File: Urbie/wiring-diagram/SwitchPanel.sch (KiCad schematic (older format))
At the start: 12 parts

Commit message: Organizing relay box sheet
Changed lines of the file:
@@
 	8000 3650 5900 3650
-Wire Wire Line
-	6300 3350 7400 3350
-Wire Wire Line
-	7400 3350 7400 3300
-Wire Wire Line
-	7400 3300 7350 3300
-Wire Wire Line
-	7350 3300 7350 3350
-Connection ~ 7350 3350
 Wire Wire Line
 	5800 3000 5800 3750
@@
 Wire Wire Line
 	6300 1850 6300 3350
-Wire Wire Line
-	8500 2250 8500 2250
 Wire Wire Line
 	7200 1300 7200 2250
@@
 Text Label 8650 2850 2    60   ~ 0
 EFI
+Wire Wire Line
+	6300 3350 7350 3350
 $EndSCHEMATC

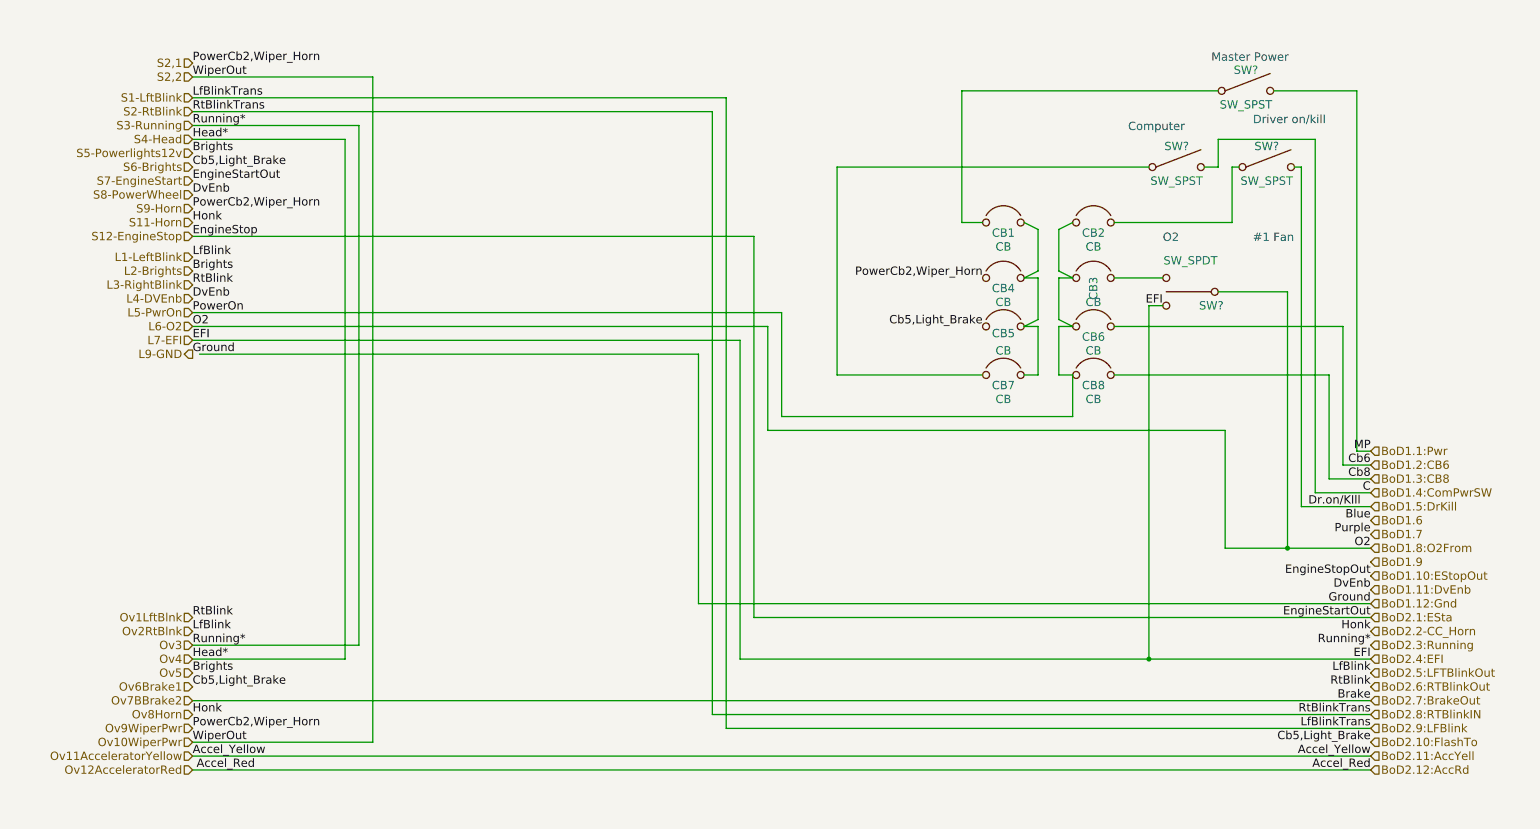
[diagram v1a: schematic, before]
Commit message: cleaning up schematics
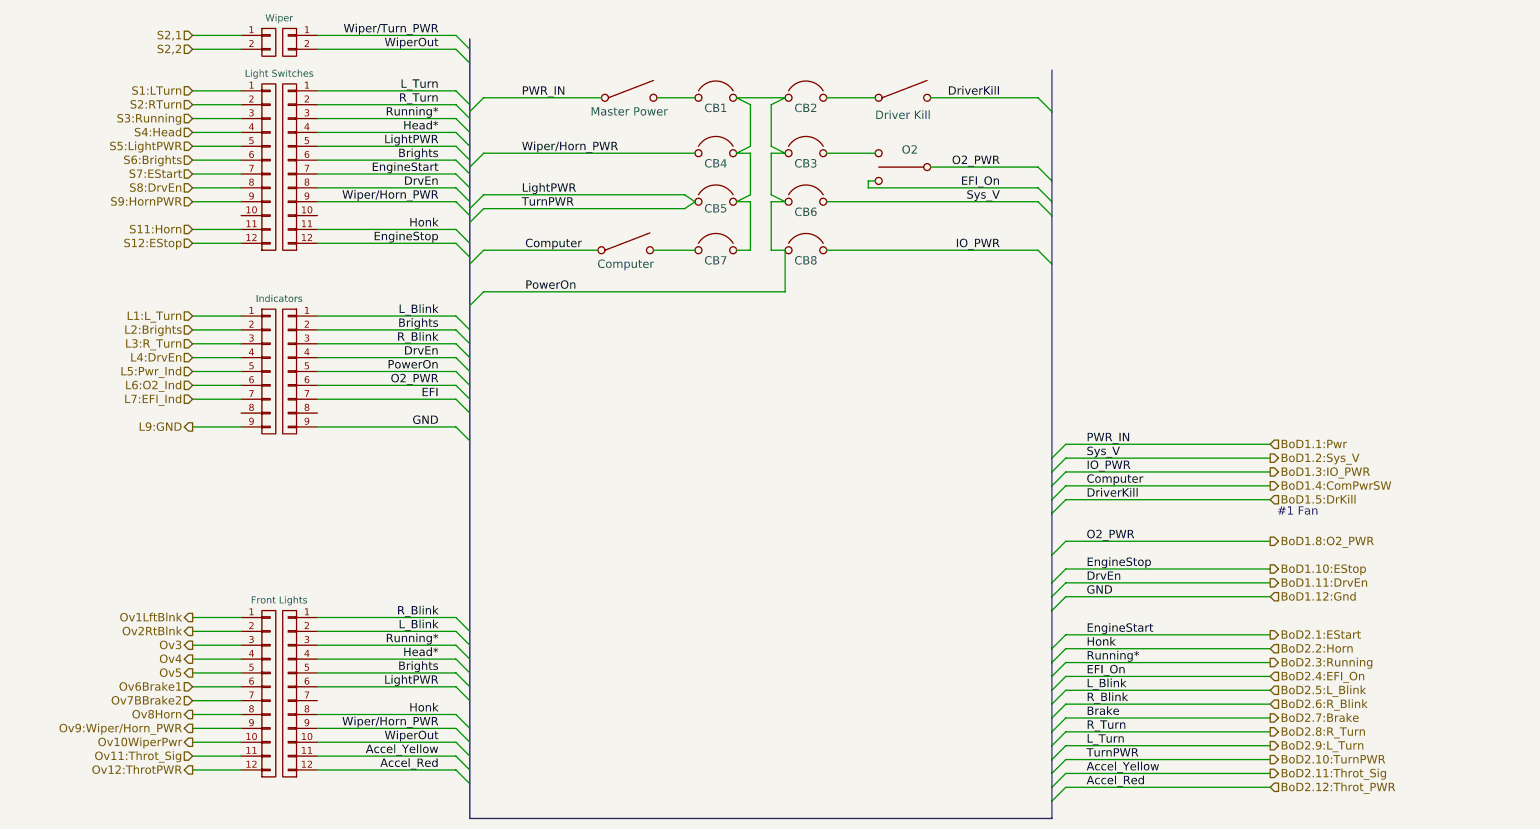
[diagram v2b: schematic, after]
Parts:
- added P?: CONN_01X09, symbol CONN_01X09
- added P?: Indicators, symbol CONN_01X09
- added P? (x2): CONN_01X12, symbol CONN_01X12
- added P?: Light Switches, symbol CONN_01X12
- added P?: CONN_01X02, symbol CONN_01X02
- added P?: Wiper, symbol CONN_01X02
- added P?: Front Lights, symbol CONN_01X12
- SW?: value SW_SPST -> Master Power
- SW?: value SW_SPST -> Computer
- SW?: value SW_SPST -> Driver Kill
- SW?: value SW_SPDT -> O2
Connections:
- net L5-PwrOn is gone; now on net PowerOn: CB2.1 (Line), CB3.1 (Line), CB6.1 (Line), CB8.1 (Line)
- net BoD1.12:Gnd: now also P?.9 (P9)
- net BoD1.1:Pwr: now also SW?.1; no longer SW?.2
- net BoD1.4:ComPwrSW: now also SW?.1; no longer SW?.2
- net BoD2.3:Running: now also P?.3 (P3), P?.3 (P3)
- net Ov10WiperPwr: now also P?.10 (P10)
- net Ov4: now also P?.4 (P4)
- net at CB1.1 (Line): now also SW?.2; no longer SW?.1
- net PowerOn: now reaches CB1.2 (Load), CB4.2 (Load), CB5.2 (Load), CB7.2 (Load)
- net PowerOn: now also P?.5 (P5)
- net at CB7.1 (Line): now also SW?.2; no longer SW?.1
- net BoD1.2:CB6 renamed BoD1.2:Sys_V
- net BoD1.3:CB8 renamed BoD1.3:IO_PWR
- net BoD1.8:O2From renamed BoD1.8:O2_PWR
- net BoD1.8:O2_PWR: now also P?.6 (P6)
- net BoD2.10:FlashTo renamed BoD2.10:TurnPWR
- net BoD2.10:TurnPWR: now also P?.5 (P5), P?.6 (P6)
- net BoD2.4:EFI renamed BoD2.4:EFI_On
- net Ov9WiperPwr renamed Wiper/Horn_PWR
- net Wiper/Horn_PWR: now also P?.9 (P9), P?.9 (P9)
- new net BoD1.10:EStop: P?.12 (P12)
- new net BoD1.11:DrvEn: P?.4 (P4), P?.8 (P8)
- new net BoD2.11:Throt_Sig: P?.11 (P11)
- new net BoD2.12:Throt_PWR: P?.12 (P12)
- new net BoD2.1:EStart: P?.7 (P7)
- new net BoD2.2:Horn: P?.11 (P11), P?.8 (P8)
- new net BoD2.5:L_Blink: P?.1 (P1), P?.2 (P2)
- new net BoD2.6:R_Blink: P?.1 (P1), P?.3 (P3)
- new net BoD2.8:R_Turn: P?.2 (P2)
- new net BoD2.9:L_Turn: P?.1 (P1)
- new net Brights: P?.2 (P2), P?.5 (P5), P?.6 (P6)
- new net EFI: P?.7 (P7)
- new net Head*: P?.4 (P4), P?.4 (P4)
- new net L1:L_Turn: P?.1 (P1)
- new net L2:Brights: P?.2 (P2)
- new net L3:R_Turn: P?.3 (P3)
- new net L4:DrvEn: P?.4 (P4)
- new net L5:Pwr_Ind: P?.5 (P5)
- new net L6:O2_Ind: P?.6 (P6)
- new net L7:EFI_Ind: P?.7 (P7)
- new net L9:GND: P?.9 (P9)
- new net Ov11:Throt_Sig: P?.11 (P11)
- new net Ov12:ThrotPWR: P?.12 (P12)
- new net Ov1LftBlnk: P?.1 (P1)
- new net Ov2RtBlnk: P?.2 (P2)
- new net Ov3: P?.3 (P3)
- new net Ov5: P?.5 (P5)
- new net Ov6Brake1: P?.6 (P6)
- new net Ov7BBrake2: P?.7 (P7)
- new net Ov8Horn: P?.8 (P8)
- new net Ov9:Wiper/Horn_PWR: P?.9 (P9)
- new net S11:Horn: P?.11 (P11)
- new net S12:EStop: P?.12 (P12)
- new net S1:LTurn: P?.1 (P1)
- new net S2,1: P?.1 (P1)
- new net S2,2: P?.2 (P2)
- new net S2:RTurn: P?.2 (P2)
- new net S3:Running: P?.3 (P3)
- new net S4:Head: P?.4 (P4)
- new net S5:LightPWR: P?.5 (P5)
- new net S6:Brights: P?.6 (P6)
- new net S7:EStart: P?.7 (P7)
- new net S8:DrvEn: P?.8 (P8)
- new net S9:HornPWR: P?.9 (P9)
- new net Wiper/Turn_PWR: P?.1 (P1)
- new net WiperOut: P?.10 (P10), P?.2 (P2)
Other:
- note removed: "Computer"
- note removed: "Driver on/kill"
- note removed: "Master Power"
- note removed: "O2"
- moved on the sheet: CB1, CB2, CB3, CB4, CB5, CB6, CB7, CB8

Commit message: fixed some stuff
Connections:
- net BoD2.7:Brake: now also P?.7 (P7)
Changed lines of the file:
@@
 $Descr USLetter 11000 8500
 encoding utf-8
-Sheet 9 9
+Sheet 9 13
 Title "Urbie - Switch Panel"
 Date "2017-01-07"
@@
 Wire Wire Line
 	2550 6000 3550 6000
+Text Label 3425 5700 2    60   ~ 0
+Brake
+Wire Wire Line
+	2550 5700 3550 5700
+Entry Wire Line
+	3550 5700 3650 5800
 $EndSCHEMATC

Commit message: updated 1593BB-box footprint
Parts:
- removed P?: CONN_01X12, symbol CONN_01X12
- removed P?: Front Lights, symbol CONN_01X12
- added P? (x2): CONN_01X15, symbol CONN_01X15
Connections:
- net BoD1.12:Gnd: now also P?.13 (P13), P?.14 (P14), P?.15 (P15)
- net BoD2.10:TurnPWR: now also P?.6 (P6)
- net BoD2.11:Throt_Sig: now also P?.11 (P11)
- net BoD2.12:Throt_PWR: now also P?.12 (P12)
- net BoD2.2:Horn: now also P?.8 (P8)
- net BoD2.3:Running: now also P?.3 (P3)
- net BoD2.5:L_Blink: now also P?.2 (P2)
- net BoD2.6:R_Blink: now also P?.1 (P1)
- net BoD2.7:Brake: now also P?.7 (P7)
- net Brights: now also P?.5 (P5)
- net Head*: now also P?.4 (P4)
- net Ov10WiperPwr: now also P?.10 (P10)
- net Ov11:Throt_Sig: now also P?.11 (P11)
- net Ov12:ThrotPWR: now also P?.12 (P12)
- net Ov1LftBlnk: now also P?.1 (P1)
- net Ov2RtBlnk: now also P?.2 (P2)
- net Ov3: now also P?.3 (P3)
- net Ov4: now also P?.4 (P4)
- net Ov5: now also P?.5 (P5)
- net Ov6Brake1: now also P?.6 (P6)
- net Ov7BBrake2: now also P?.7 (P7)
- net Ov8Horn: now also P?.8 (P8)
- net Ov9:Wiper/Horn_PWR: now also P?.9 (P9)
- net Wiper/Horn_PWR: now also P?.9 (P9)
- net WiperOut: now also P?.10 (P10)
- new net Ov13:GND: P?.13 (P13)
- new net Ov14:GND: P?.14 (P14)
- new net Ov15:GND: P?.15 (P15)
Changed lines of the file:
@@
 $Descr USLetter 11000 8500
 encoding utf-8
-Sheet 9 13
+Sheet 13 13
 Title "Urbie - Switch Panel"
 Date "2017-01-07"
@@
 Comment4 ""
 $EndDescr
+Text HLabel 1650 4900 0    60   Output ~ 0
+Ov1LftBlnk
+Text HLabel 1650 5000 0    60   Output ~ 0
+Ov2RtBlnk
 Text HLabel 1650 5100 0    60   Output ~ 0
-Ov1LftBlnk
+Ov3
 Text HLabel 1650 5200 0    60   Output ~ 0
-Ov2RtBlnk
+Ov4
 Text HLabel 1650 5300 0    60   Output ~ 0
-Ov3
-Text HLabel 1650 5400 0    60   Output ~ 0
-Ov4
-Text HLabel 1650 5500 0    60   Output ~ 0
 Ov5
-Text HLabel 1650 5600 0    60   Input ~ 0
+Text HLabel 1650 5400 0    60   Input ~ 0
 Ov6Brake1
-Text HLabel 1650 5700 0    60   Input ~ 0
+Text HLabel 1650 5500 0    60   Input ~ 0
 Ov7BBrake2
+Text HLabel 1650 5600 0    60   Output ~ 0
+Ov8Horn
+Text HLabel 1650 5700 0    60   Output ~ 0
+Ov9:Wiper/Horn_PWR
 Text HLabel 1650 5800 0    60   Output ~ 0
-Ov8Horn
-Text HLabel 1650 5900 0    60   Output ~ 0
-Ov9:Wiper/Horn_PWR
+Ov10WiperPwr
+Text HLabel 1650 5900 0    60   Input ~ 0
+Ov11:Throt_Sig
 Text HLabel 1650 6000 0    60   Output ~ 0
-Ov10WiperPwr
-Text HLabel 1650 6100 0    60   Input ~ 0
-Ov11:Throt_Sig
-Text HLabel 1650 6200 0    60   Output ~ 0
 Ov12:ThrotPWR
 Text HLabel 1650 2925 0    60   Input ~ 0
@@
 Text Label 3425 1700 2    60   ~ 0
 LightPWR
-Text Label 3425 5600 2    60   ~ 0
+Text Label 3425 5400 2    60   ~ 0
 LightPWR
 Text Label 8100 6125 0    60   ~ 0
@@
 Text Label 3425 2300 2    60   ~ 0
 Honk
-Text Label 3425 5800 2    60   ~ 0
+Text Label 3425 5600 2    60   ~ 0
 Honk
 Text Label 8100 5325 0    60   ~ 0
@@
 Text Label 3425 2925 2    60   ~ 0
 L_Blink
-Text Label 3425 5200 2    60   ~ 0
+Text Label 3425 5000 2    60   ~ 0
 L_Blink
 Text Label 8100 5625 0    60   ~ 0
@@
 Text Label 3425 3025 2    60   ~ 0
 Brights
-Text Label 3425 5500 2    60   ~ 0
+Text Label 3425 5300 2    60   ~ 0
 Brights
-Text Label 3425 5100 2    60   ~ 0
+Text Label 3425 4900 2    60   ~ 0
 R_Blink
 Text Label 3425 3125 2    60   ~ 0
@@
 Text Label 3425 1500 2    60   ~ 0
 Running*
-Text Label 3425 5300 2    60   ~ 0
+Text Label 3425 5100 2    60   ~ 0
 Running*
 Text Label 8100 5425 0    60   ~ 0
@@
 Text Label 3425 1600 2    60   ~ 0
 Head*
-Text Label 3425 5400 2    60   ~ 0
+Text Label 3425 5200 2    60   ~ 0
 Head*
-Text Label 3425 5900 2    60   ~ 0
+Text Label 3425 5700 2    60   ~ 0
 Wiper/Horn_PWR
 Text Label 3425 1000 2    60   ~ 0
 WiperOut
-Text Label 3425 6000 2    60   ~ 0
+Text Label 3425 5800 2    60   ~ 0
 WiperOut
 Text Label 8100 4750 0    60   ~ 0
@@
 Text Label 8100 6325 0    60   ~ 0
 Accel_Red
-Text Label 3425 6200 2    60   ~ 0
+Text Label 3425 6000 2    60   ~ 0
 Accel_Red
-Text Label 3425 6100 2    60   ~ 0
+Text Label 3425 5900 2    60   ~ 0
 Accel_Yellow
 Text Label 3425 2400 2    60   ~ 0
@@
 	3550 3725 3650 3825
 Entry Wire Line
+	3550 4900 3650 5000
+Entry Wire Line
+	3550 5000 3650 5100
+Entry Wire Line
 	3550 5100 3650 5200
 Entry Wire Line
@@
 	3550 5400 3650 5500
 Entry Wire Line
-	3550 5500 3650 5600
-Entry Wire Line
 	3550 5600 3650 5700
 Entry Wire Line
+	3550 5700 3650 5800
+Entry Wire Line
 	3550 5800 3650 5900
 Entry Wire Line
@@
 Entry Wire Line
 	3550 6000 3650 6100
-Entry Wire Line
-	3550 6100 3650 6200
-Entry Wire Line
-	3550 6200 3650 6300
 $Comp
 L CONN_01X09 P?
@@
 Wire Wire Line
 	2000 1000 1650 1000
-$Comp
-L CONN_01X12 P?
-U 1 1 58784560
-P 2350 5650
-F 0 "P?" H 2350 6300 50  0001 C CNN
-F 1 "CONN_01X12" V 2450 5650 50  0001 C CNN
-F 2 "" H 2350 5650 50  0000 C CNN
-F 3 "" H 2350 5650 50  0000 C CNN
-	1    2350 5650
+Wire Wire Line
+	2550 4900 3550 4900
+Wire Wire Line
+	2550 5000 3550 5000
+Wire Wire Line
+	2550 5100 3550 5100
+Wire Wire Line
+	2550 5200 3550 5200
+Wire Wire Line
+	2550 5300 3550 5300
+Wire Wire Line
+	2550 5400 3550 5400
+Wire Wire Line
+	2550 5600 3550 5600
+Wire Wire Line
+	2550 5700 3550 5700
+Wire Wire Line
+	2550 5900 3550 5900
+Wire Wire Line
+	2550 6000 3550 6000
+Wire Wire Line
+	2000 6000 1650 6000
+Wire Wire Line
+	1650 5900 2000 5900
+Wire Wire Line
+	1650 5700 2000 5700
+Wire Wire Line
+	1650 5600 2000 5600
+Wire Wire Line
+	1650 5500 2000 5500
+Wire Wire Line
+	1650 5400 2000 5400
+Wire Wire Line
+	1650 5300 2000 5300
+Wire Wire Line
+	1650 5200 2000 5200
+Wire Wire Line
+	1650 5100 2000 5100
+Wire Wire Line
+	1650 5000 2000 5000
+Wire Wire Line
+	1650 4900 2000 4900
+Wire Wire Line
+	2000 5800 1650 5800
+Wire Wire Line
+	2550 5800 3550 5800
+Text Label 3425 5500 2    60   ~ 0
+Brake
+Wire Wire Line
+	2550 5500 3550 5500
+Entry Wire Line
+	3550 5500 3650 5600
+$Comp
+L CONN_01X15 P?
+U 1 1 5891B89E
+P 2200 5600
+F 0 "P?" H 2200 6400 50  0000 C CNN
+F 1 "CONN_01X15" V 2300 5600 50  0001 C CNN
+F 2 "" H 2200 5600 50  0000 C CNN
+F 3 "" H 2200 5600 50  0000 C CNN
+	1    2200 5600
+	1    0    0    -1
+$EndComp
+$Comp
+L CONN_01X15 P?
+U 1 1 5891BDDD
+P 2350 5600
+F 0 "P?" H 2350 6400 50  0000 C CNN
+F 1 "CONN_01X15" V 2450 5600 50  0001 C CNN
+F 2 "" H 2350 5600 50  0000 C CNN
+F 3 "" H 2350 5600 50  0000 C CNN
+	1    2350 5600
 	-1   0    0    -1
 $EndComp
-$Comp
-L CONN_01X12 P?
-U 1 1 58784566
-P 2200 5650
-F 0 "P?" H 2200 6300 50  0001 C CNN
-F 1 "Front Lights" H 2275 6325 50  0000 C CNN
-F 2 "" H 2200 5650 50  0000 C CNN
-F 3 "" H 2200 5650 50  0000 C CNN
-	1    2200 5650
-	1    0    0    -1
-$EndComp
-Wire Wire Line
-	2550 5100 3550 5100
-Wire Wire Line
-	2550 5200 3550 5200
-Wire Wire Line
-	2550 5300 3550 5300
-Wire Wire Line
-	2550 5400 3550 5400
-Wire Wire Line
-	2550 5500 3550 5500
-Wire Wire Line
-	2550 5600 3550 5600
-Wire Wire Line
-	2550 5800 3550 5800
-Wire Wire Line
-	2550 5900 3550 5900
+Text Label 3250 6100 0    60   ~ 0
+GND
+Text Label 3250 6200 0    60   ~ 0
+GND
+Text Label 3250 6300 0    60   ~ 0
+GND
 Wire Wire Line
 	2550 6100 3550 6100
@@
 	2550 6200 3550 6200
 Wire Wire Line
-	2000 6200 1650 6200
+	2550 6300 3550 6300
+Entry Wire Line
+	3550 6100 3650 6200
+Entry Wire Line
+	3550 6200 3650 6300
+Entry Wire Line
+	3550 6300 3650 6400
+Text HLabel 1650 6200 0    60   Output ~ 0
+Ov14:GND
+Text HLabel 1650 6300 0    60   Output ~ 0
+Ov15:GND
+Wire Wire Line
+	1650 6300 2000 6300
+Wire Wire Line
+	1650 6200 2000 6200
 Wire Wire Line
 	1650 6100 2000 6100
-Wire Wire Line
-	1650 5900 2000 5900
-Wire Wire Line
-	1650 5800 2000 5800
-Wire Wire Line
-	1650 5700 2000 5700
-Wire Wire Line
-	1650 5600 2000 5600
-Wire Wire Line
-	1650 5500 2000 5500
-Wire Wire Line
-	1650 5400 2000 5400
-Wire Wire Line
-	1650 5300 2000 5300
-Wire Wire Line
-	1650 5200 2000 5200
-Wire Wire Line
-	1650 5100 2000 5100
-Wire Wire Line
-	2000 6000 1650 6000
-Wire Wire Line
-	2550 6000 3550 6000
-Text Label 3425 5700 2    60   ~ 0
-Brake
-Wire Wire Line
-	2550 5700 3550 5700
-Entry Wire Line
-	3550 5700 3650 5800
+Text HLabel 1650 6100 0    60   Output ~ 0
+Ov13:GND
 $EndSCHEMATC
